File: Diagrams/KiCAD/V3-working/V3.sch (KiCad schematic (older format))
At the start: 41 parts, among them U2 NodeMCU_1.0_(ESP-12E), U3 74HC595, U4 74HC595

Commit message: Diagram updates.
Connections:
- net labels removed: d
- wire segments 227 -> 191
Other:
- note added: "Delete wires as they\nare completed."
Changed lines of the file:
@@
 Connection ~ 3300 2100
-Wire Wire Line
-	3300 2100 3300 2650
 Wire Wire Line
 	3750 1800 3750 2250
@@
 	3750 2650 3800 2650
 Wire Wire Line
-	3450 2650 3300 2650
-Connection ~ 3300 2650
-Wire Wire Line
-	3300 2650 3300 2850
-Wire Wire Line
 	3800 2500 3800 2650
-Connection ~ 3800 2650
-Wire Wire Line
-	3800 2650 4200 2650
 Wire Wire Line
 	3750 2850 3800 2850
 Wire Wire Line
-	3450 2850 3300 2850
-Connection ~ 3300 2850
-Wire Wire Line
-	3300 2850 3300 3050
-Wire Wire Line
 	3800 2950 3800 2850
-Connection ~ 3800 2850
-Wire Wire Line
-	3800 2850 4200 2850
-Wire Wire Line
-	3450 3650 3300 3650
-Connection ~ 3300 3650
 Wire Wire Line
 	3750 3650 3800 3650
 Wire Wire Line
 	3800 3450 3800 3650
-Connection ~ 3800 3650
-Wire Wire Line
-	3800 3650 4200 3650
 Connection ~ 3300 4400
 Wire Wire Line
@@
 Connection ~ 6650 3100
 Wire Wire Line
-	5800 2750 6450 2750
-Wire Wire Line
 	7250 2750 7250 2700
-Wire Wire Line
-	6450 2750 6450 3900
-Wire Wire Line
-	6450 4400 7250 4400
-Connection ~ 6450 2750
-Wire Wire Line
-	6450 2750 7250 2750
-Wire Wire Line
-	6850 2200 6450 2200
-Wire Wire Line
-	6450 2200 6450 2750
-Wire Wire Line
-	6850 3900 6450 3900
-Connection ~ 6450 3900
-Wire Wire Line
-	6450 3900 6450 4400
 Wire Wire Line
 	4200 3450 4000 3450
@@
 	1850 3250 3300 3250
 Connection ~ 3300 3250
-Wire Wire Line
-	3300 3250 3300 3650
-Wire Wire Line
-	3300 3650 3300 4400
 Text Label 1350 2550 1    50   ~ 0
 12V
@@
 Wire Wire Line
 	8350 1900 8800 1900
-Wire Wire Line
-	7650 1600 7850 1600
-Wire Wire Line
-	7650 1700 7850 1700
-Wire Wire Line
-	7650 1800 7850 1800
-Wire Wire Line
-	7650 1900 7850 1900
 Text Label 8400 1600 0    50   ~ 0
 BR
@@
 	1    0    0    -1
 $EndComp
-Wire Wire Line
-	7650 2000 7850 2000
-Wire Wire Line
-	7650 2100 7850 2100
-Wire Wire Line
-	7650 2200 7850 2200
-Wire Wire Line
-	7650 2300 7850 2300
 Wire Wire Line
 	7600 1200 7850 1200
@@
 Wire Wire Line
 	8450 5100 8800 5100
-Wire Wire Line
-	7650 3600 7700 3600
-Wire Wire Line
-	7700 3600 7700 5100
-Wire Wire Line
-	7700 5100 8000 5100
-Wire Wire Line
-	7650 3500 7750 3500
-Wire Wire Line
-	7750 3500 7750 5000
-Wire Wire Line
-	7750 5000 8000 5000
-Wire Wire Line
-	7650 3400 7800 3400
-Wire Wire Line
-	7800 3400 7800 4900
-Wire Wire Line
-	7800 4900 8000 4900
-Wire Wire Line
-	7650 3300 7850 3300
-Wire Wire Line
-	7850 3300 7850 4800
-Wire Wire Line
-	7850 4800 8000 4800
 $Comp
 L Connector:Conn_01x02_Female J?
@@
 Text Label 8150 4050 0    50   ~ 0
 GND
-Text Label 3925 2680 0    50   ~ 0
-d
-Text Label 3925 2880 0    50   ~ 0
-d
-Text Label 3925 3675 0    50   ~ 0
-d
-Text Label 3275 2780 0    50   ~ 0
-d
-Text Label 3275 3575 0    50   ~ 0
-d
-Text Label 6865 4425 0    50   ~ 0
-d
-Text Label 6905 2780 0    50   ~ 0
-d
-Text Label 6755 2230 0    50   ~ 0
-d
-Text Label 6695 3930 0    50   ~ 0
-d
+Wire Wire Line
+	5805 2750 6025 2750
+Text Label 5845 2750 0    50   ~ 0
+GND
+Text Label 3795 3045 0    50   ~ 0
+GND
+Text Label 3720 2355 0    50   ~ 0
+GND
+Wire Wire Line
+	3300 2100 3300 3050
+Wire Wire Line
+	3300 3250 3300 4400
+Text Notes 1060 1000 0    157  ~ 0
+Delete wires as they\nare completed.
 $EndSCHEMATC

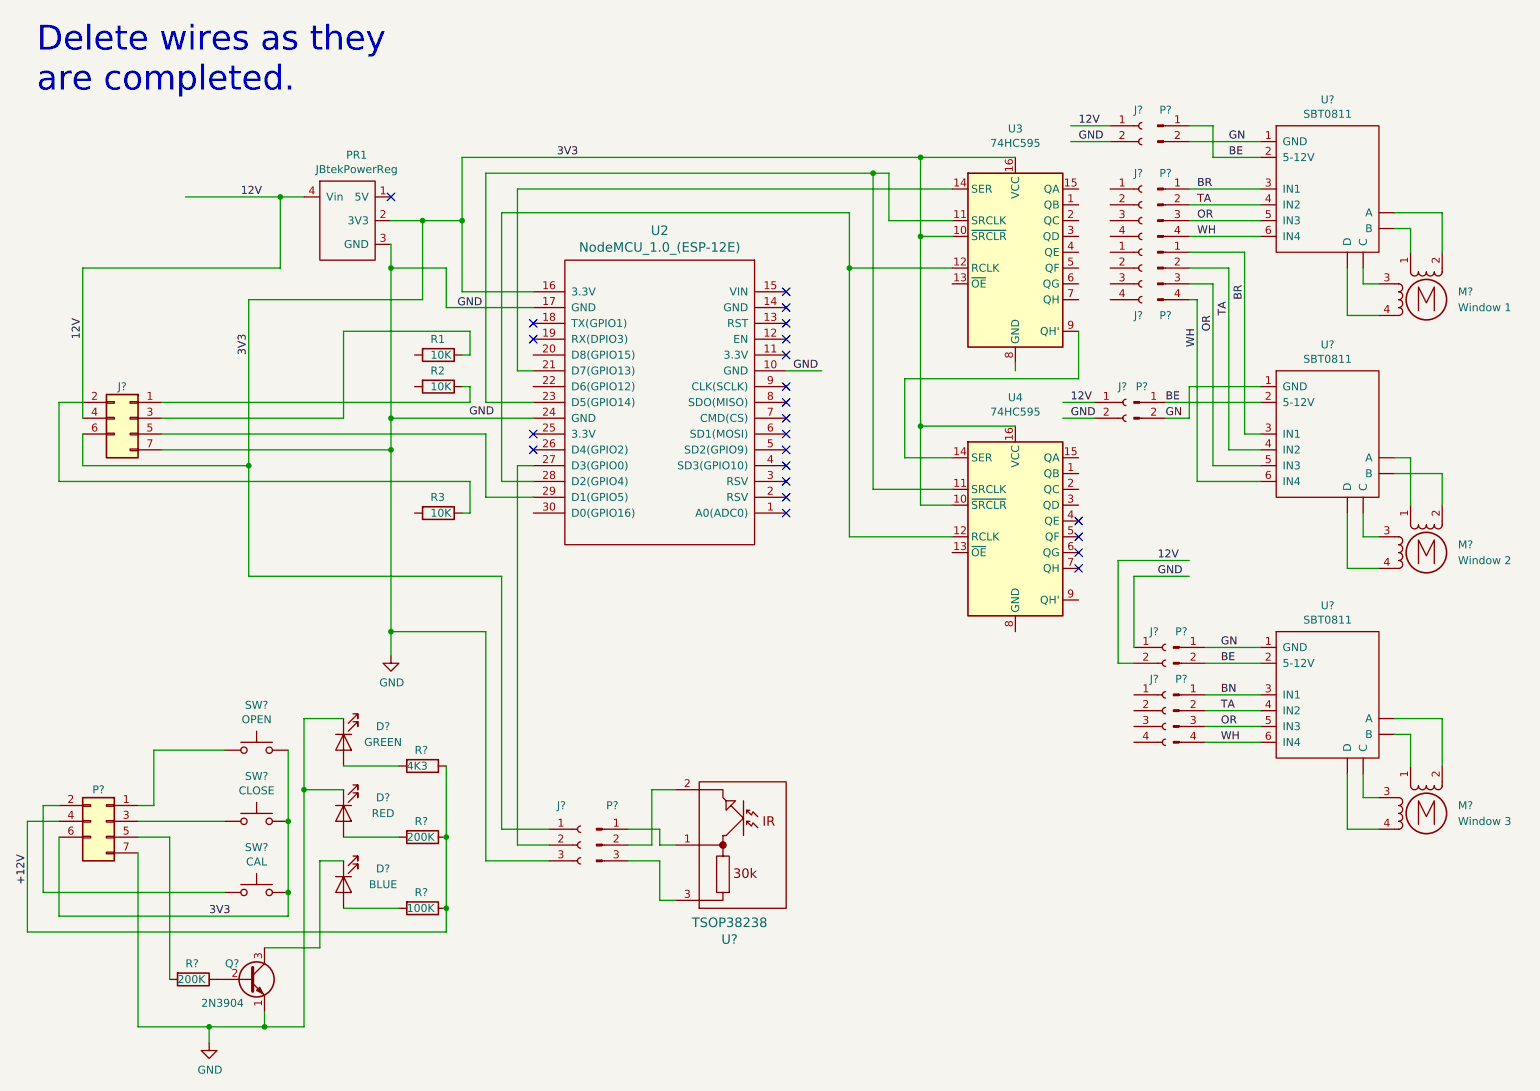
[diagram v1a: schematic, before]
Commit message: Abandoned approach of deleting wires in diagram as they are completed. The resultant schematic becomes too hard to follow. Now marking completed connections with a period.
Added colors to switchboard jack and plug in diagram to minimize
confusion. Still would be useful to have a diagram of the physical
connector on the board.
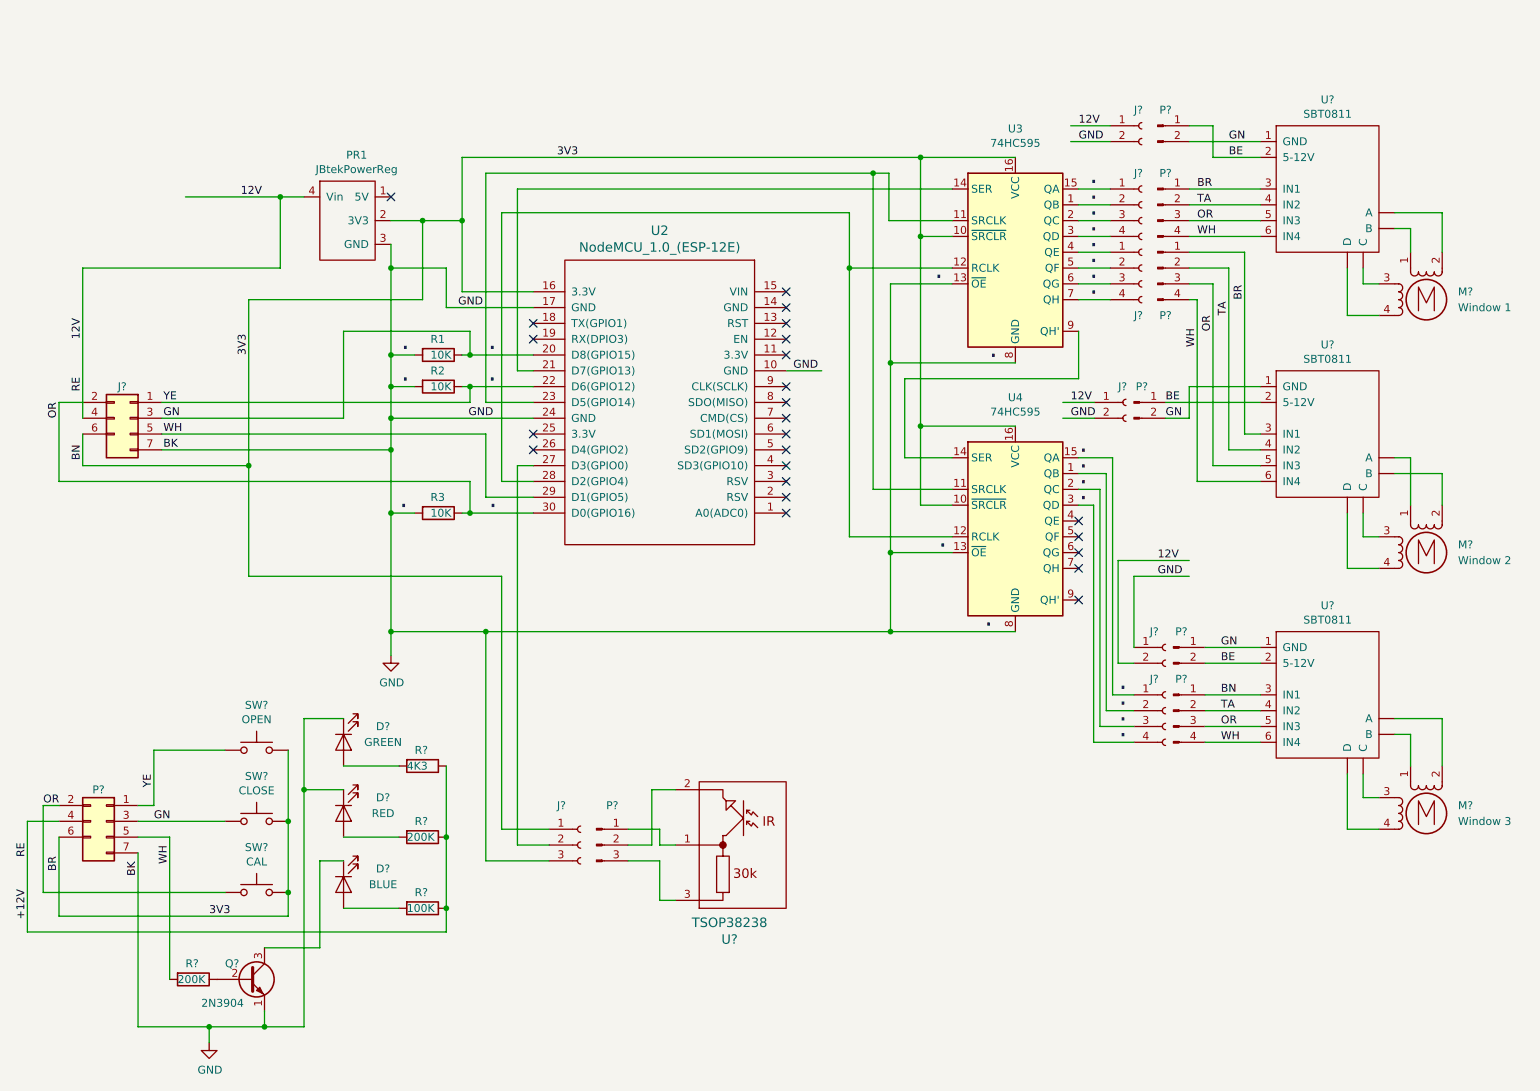
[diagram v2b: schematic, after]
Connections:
- net labels added: ., BK, RE, YE
- wire segments 191 -> 227
- no-connect marks 23 -> 24
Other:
- note removed: "Delete wires as they\nare completed."
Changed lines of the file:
@@
 Connection ~ 6650 3100
-Wire Wire Line
-	7250 2750 7250 2700
 Wire Wire Line
 	4200 3450 4000 3450
@@
 	3650 5250 3650 5700
 Connection ~ 3650 5700
-Text Label 1000 6000 1    50   ~ 0
+Text Label 1000 6220 1    50   ~ 0
 +12V
 $Comp
@@
 Wire Wire Line
 	8350 4050 8000 4050
-Wire Wire Line
-	8000 4050 8000 4500
 Text Label 8150 3950 0    50   ~ 0
 12V
@@
 Text Label 5845 2750 0    50   ~ 0
 GND
-Text Label 3795 3045 0    50   ~ 0
+Text Label 3790 3050 0    50   ~ 0
 GND
-Text Label 3720 2355 0    50   ~ 0
+Text Label 3725 2350 0    50   ~ 0
 GND
 Wire Wire Line
-	3300 2100 3300 3050
-Wire Wire Line
-	3300 3250 3300 4400
-Text Notes 1060 1000 0    157  ~ 0
-Delete wires as they\nare completed.
+	3300 2100 3300 2650
+Wire Wire Line
+	3300 3250 3300 3650
+Text Label 1860 2950 0    50   ~ 0
+YE
+Text Label 1860 3050 0    50   ~ 0
+GN
+Text Label 1860 3150 0    50   ~ 0
+WH
+Text Label 1860 3250 0    50   ~ 0
+BK
+Text Label 1200 3050 1    50   ~ 0
+OR
+Text Label 1350 2880 1    50   ~ 0
+RE
+Text Label 1350 3315 1    50   ~ 0
+BN
+Text Label 1800 5385 1    50   ~ 0
+YE
+Wire Wire Line
+	4200 2650 3800 2650
+Connection ~ 3800 2650
+Text Label 3915 2650 0    118  ~ 0
+.
+Wire Wire Line
+	4200 2850 3800 2850
+Connection ~ 3800 2850
+Wire Wire Line
+	4200 3650 3800 3650
+Connection ~ 3800 3650
+Wire Wire Line
+	8000 4050 8000 4500
+Wire Wire Line
+	7865 4800 7865 3300
+Wire Wire Line
+	7650 3300 7865 3300
+Wire Wire Line
+	7865 4800 8000 4800
+Wire Wire Line
+	7650 3400 7825 3400
+Wire Wire Line
+	7825 3400 7825 4900
+Wire Wire Line
+	7825 4900 8000 4900
+Wire Wire Line
+	7650 3500 7785 3500
+Wire Wire Line
+	7785 3500 7785 5000
+Wire Wire Line
+	7785 5000 8000 5000
+Wire Wire Line
+	7650 3600 7745 3600
+Wire Wire Line
+	7745 3600 7745 5100
+Wire Wire Line
+	7745 5100 8000 5100
+Text Label 3915 2850 0    118  ~ 0
+.
+Text Label 3920 3650 0    118  ~ 0
+.
+Text Label 7655 3300 0    118  ~ 0
+.
+Text Label 7655 3400 0    118  ~ 0
+.
+Text Label 7655 3500 0    118  ~ 0
+.
+Text Label 7655 3600 0    118  ~ 0
+.
+Text Label 7905 4800 0    118  ~ 0
+.
+Text Label 7905 4900 0    118  ~ 0
+.
+Text Label 7905 5000 0    118  ~ 0
+.
+Text Label 7905 5100 0    118  ~ 0
+.
+Wire Wire Line
+	7650 1600 7850 1600
+Wire Wire Line
+	7650 1700 7850 1700
+Wire Wire Line
+	7650 1800 7850 1800
+Wire Wire Line
+	7650 1900 7850 1900
+Wire Wire Line
+	7650 2000 7850 2000
+Wire Wire Line
+	7650 2100 7850 2100
+Wire Wire Line
+	7650 2200 7850 2200
+Wire Wire Line
+	7650 2300 7850 2300
+Text Label 7720 1600 0    118  ~ 0
+.
+Text Label 7720 1700 0    118  ~ 0
+.
+Text Label 7720 1800 0    118  ~ 0
+.
+Text Label 7720 1900 0    118  ~ 0
+.
+Text Label 7720 2000 0    118  ~ 0
+.
+Text Label 7720 2100 0    118  ~ 0
+.
+Text Label 7720 2200 0    118  ~ 0
+.
+Text Label 7720 2300 0    118  ~ 0
+.
+Wire Wire Line
+	3450 2650 3300 2650
+Connection ~ 3300 2650
+Wire Wire Line
+	3300 2650 3300 2850
+Wire Wire Line
+	3450 2850 3300 2850
+Connection ~ 3300 2850
+Wire Wire Line
+	3300 2850 3300 3050
+Text Label 3365 2650 0    118  ~ 0
+.
+Text Label 3365 2850 0    118  ~ 0
+.
+Wire Wire Line
+	3450 3650 3300 3650
+Connection ~ 3300 3650
+Wire Wire Line
+	3300 3650 3300 4400
+Text Label 3355 3650 0    118  ~ 0
+.
+Wire Wire Line
+	7250 4400 6460 4400
+Connection ~ 3900 4400
+Text Label 7055 4400 0    118  ~ 0
+.
+Wire Wire Line
+	6850 2200 6460 2200
+Wire Wire Line
+	6460 2200 6460 2700
+Connection ~ 6460 4400
+Wire Wire Line
+	6460 4400 3900 4400
+Text Label 6740 2200 0    118  ~ 0
+.
+Wire Wire Line
+	7250 2700 6460 2700
+Connection ~ 6460 2700
+Wire Wire Line
+	6460 2700 6460 3900
+Text Label 7085 2700 0    118  ~ 0
+.
+Wire Wire Line
+	6850 3900 6460 3900
+Connection ~ 6460 3900
+Wire Wire Line
+	6460 3900 6460 4400
+Text Label 6765 3900 0    118  ~ 0
+.
+Text Label 1800 5600 0    50   ~ 0
+GN
+Text Label 1900 5870 1    50   ~ 0
+WH
+Text Label 1700 5945 1    50   ~ 0
+BK
+Text Label 1100 5500 0    50   ~ 0
+OR
+Text Label 1000 5825 1    50   ~ 0
+RE
+Text Label 1200 5820 3    50   ~ 0
+BR
+NoConn ~ 7650 4200
 $EndSCHEMATC
